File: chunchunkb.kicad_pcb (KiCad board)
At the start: 2 copper layers, 143.7 x 119.1 mm, 124 parts, among them J1 BATT, J2 OLED, SW1 SW_Push, SW10 SW_Push, SW11 SW_Push, SW12 SW_Push, SW13 SW_Push, SW14 SW_Push, SW15 SW_Push, SW16 SW_Push, SW17 SW_Push, SW18 SW_Push, SW19 SW_Push, SW2 SW_Push, SW20 SW_Push, SW21 SW_Push, SW22 SW_Push, SW23 SW_Push, SW24 SW_Push, SW25 SW_Push, SW26 SW_Push, SW27 SW_Push, SW28 SW_Push, SW29 SW_Push, SW3 SW_Push, SW30 SW_Push, SW31 EC11, SW32 SW_Push, SW33 SW_Push, SW34 SW_Push, SW35 SW_Push, SW36 SW_Push, SW4 SW_Push, SW5 SW_Push, SW6 SW_Push, SW7 SW_Push, SW8 SW_Push, SW9 SW_Push

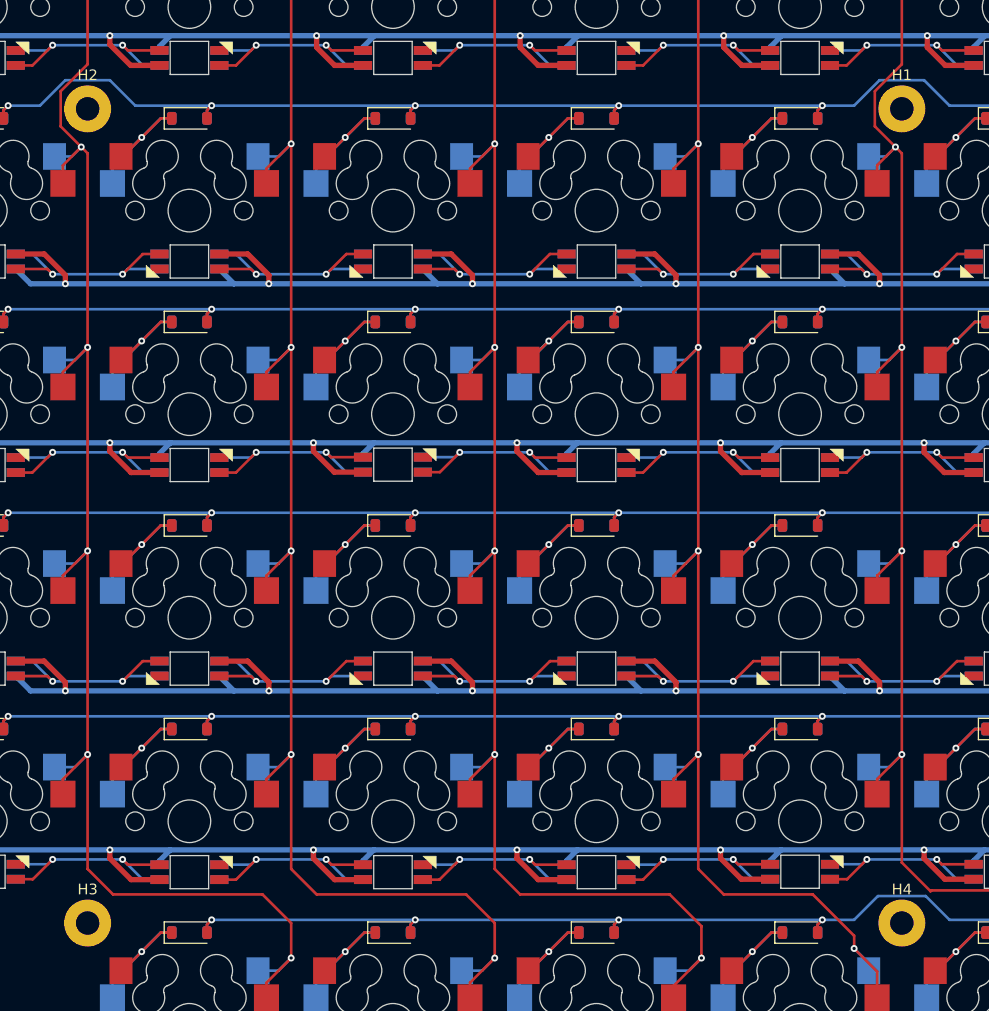
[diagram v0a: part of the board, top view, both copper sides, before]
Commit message: feat: add case
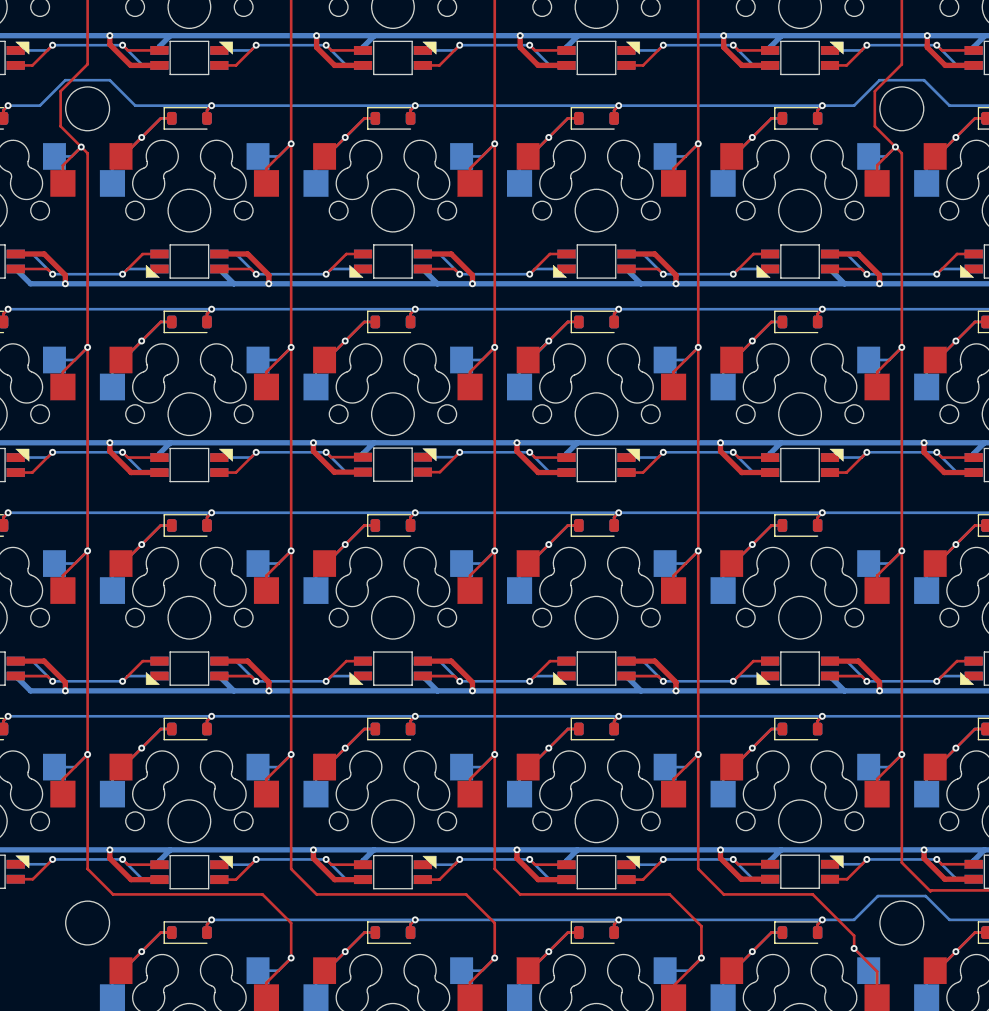
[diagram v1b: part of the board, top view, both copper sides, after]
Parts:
- H1, H2, H3, H4: footprint MountingHole:MountingHole_2.2mm_M2_Pad -> chunchunkb:HOLE_M2_TH

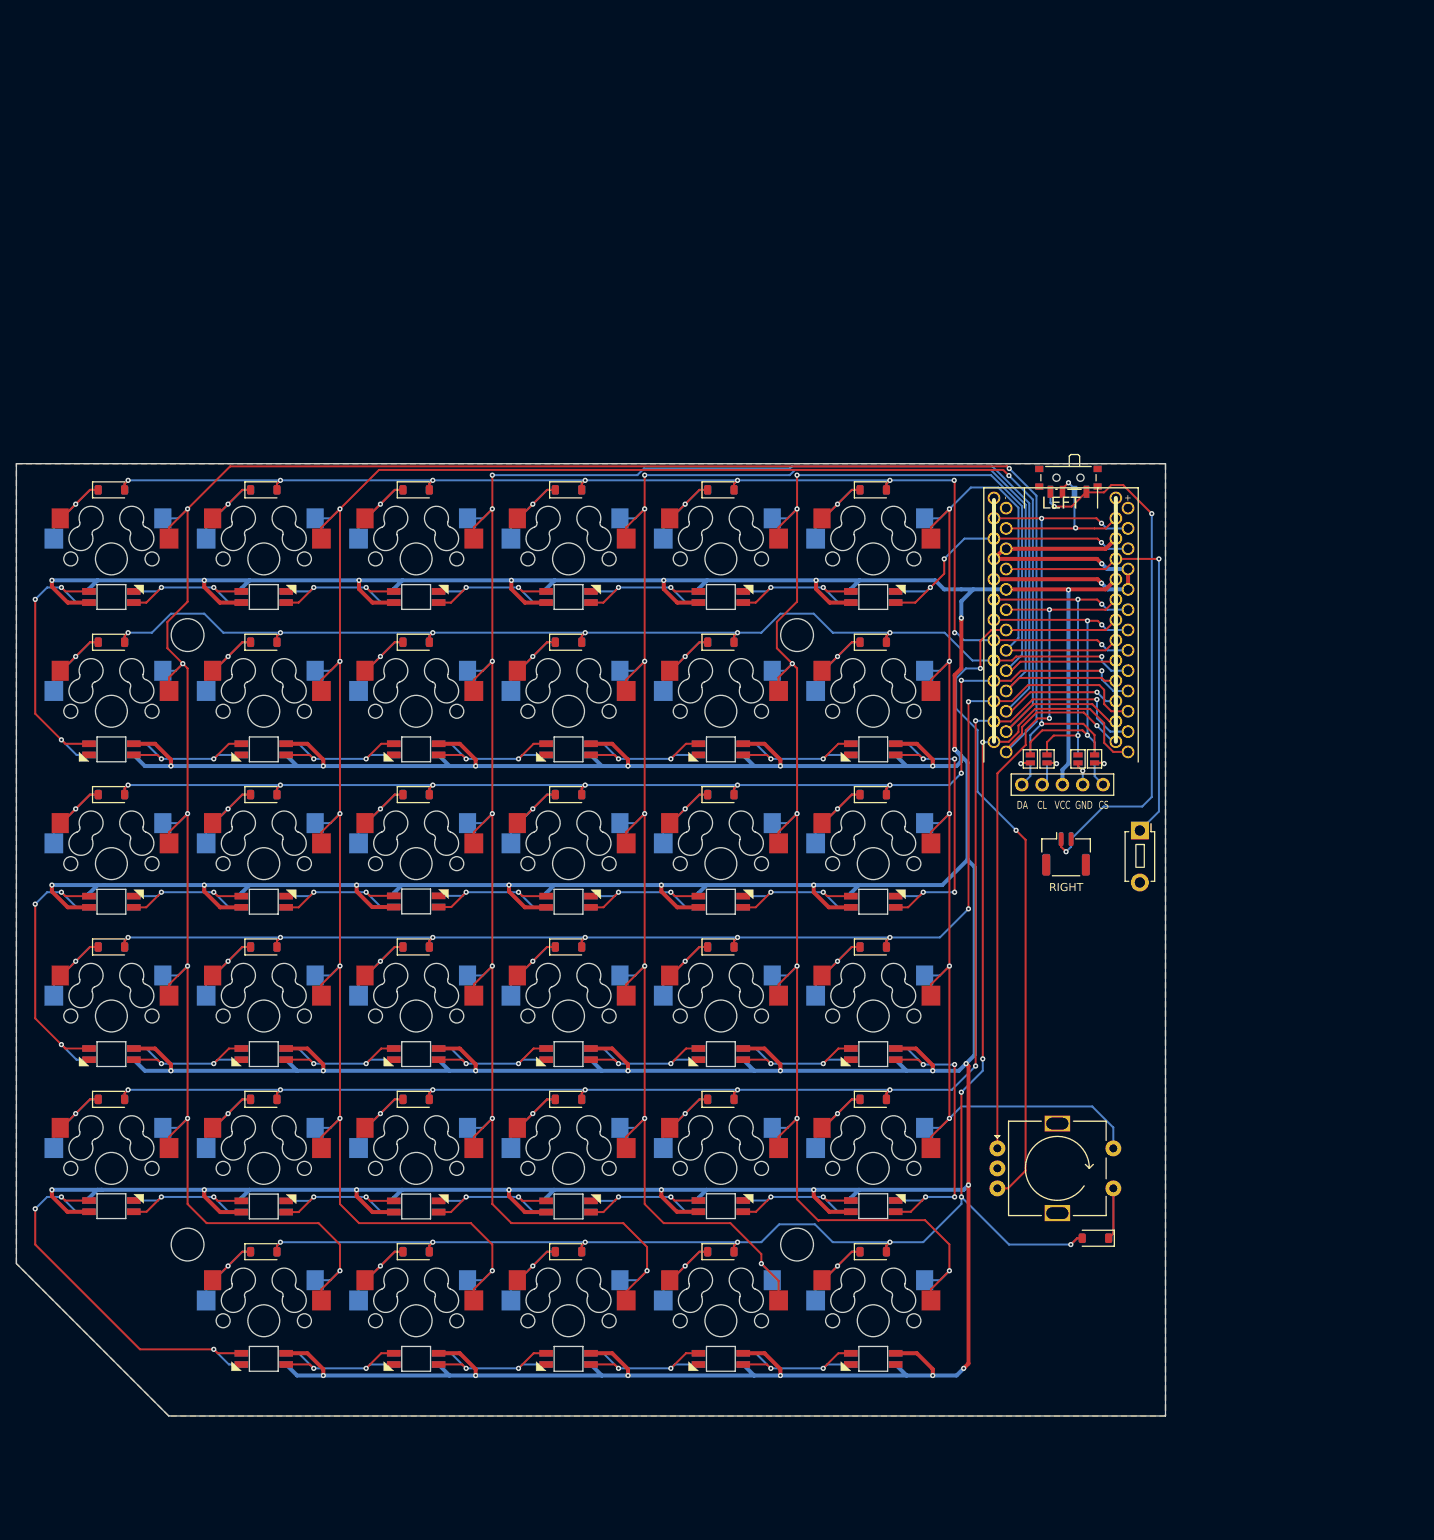
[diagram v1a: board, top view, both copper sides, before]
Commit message: feat: modular layout
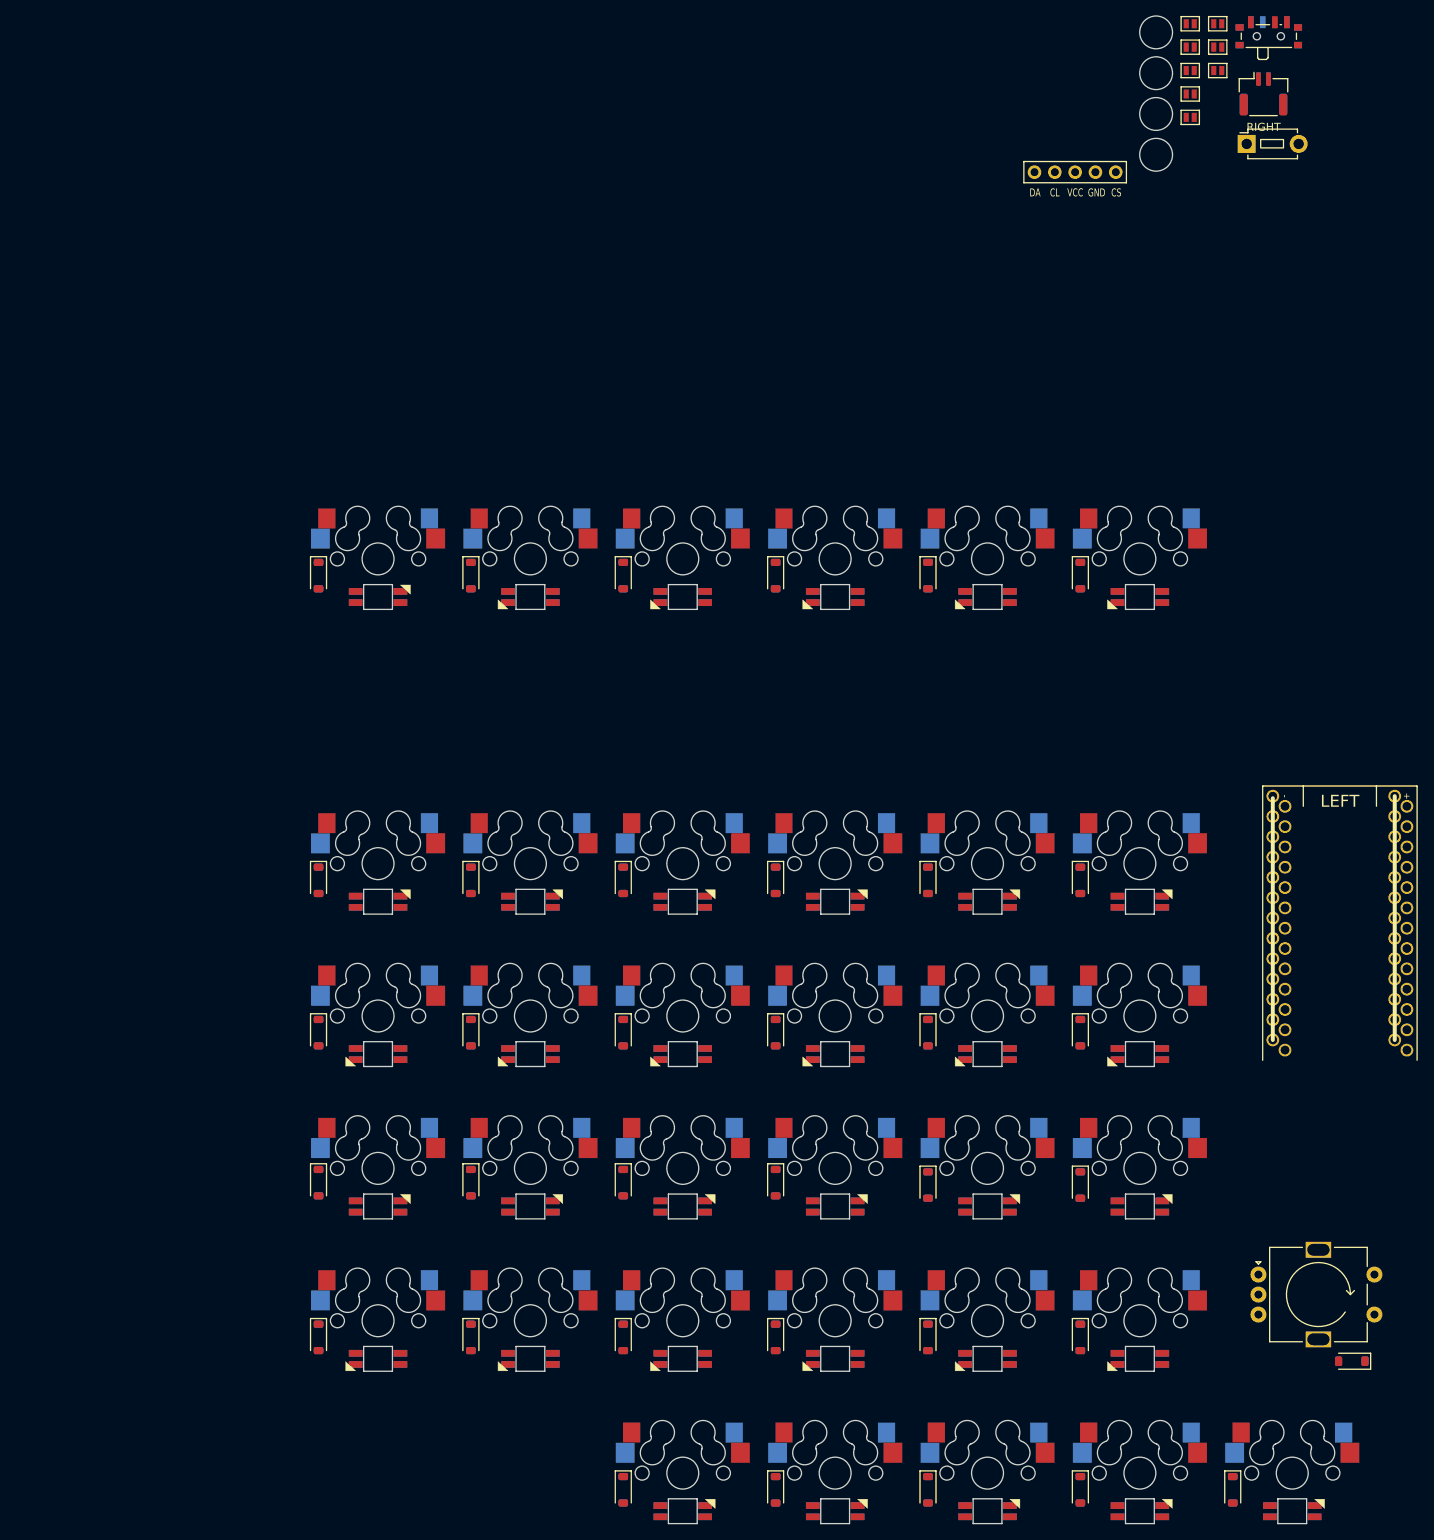
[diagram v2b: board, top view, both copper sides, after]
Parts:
- JP5, JP6, JP7, JP8: moved to F.Cu
- LED10, LED11, LED12, LED19, LED20, LED21, LED22, LED23, LED24, LED31, LED32, LED33, LED34, LED35, LED7, LED8, LED9: moved to B.Cu
- moved H3 186.1 mm to (164.0, -22.3)
- moved H4 143.5 mm to (164.0, -17.2)
- moved H2 140.0 mm to (164.0, -27.4)
- moved LED34 100.9 mm to (142.9, 38.1)
- moved LED31 100.9 mm to (85.7, 38.1)
- moved LED32 100.9 mm to (104.8, 38.1)
- moved LED33 100.9 mm to (123.8, 38.1)
- moved LED35 100.9 mm to (161.9, 38.1)
- moved J1 98.2 mm to (177.4, -24.8)
- moved JP6 94.4 mm to (171.7, -33.6), turned to 0 degrees
- moved JP1 92.7 mm to (168.2, -33.6), turned to 0 degrees
- moved JP7 90.7 mm to (171.7, -30.6), turned to 0 degrees
- moved JP2 90.1 mm to (168.2, -30.6), turned to 0 degrees
- moved JP3 87.9 mm to (168.2, -27.7), turned to 0 degrees
- moved H1 87.7 mm to (164.0, -32.5)
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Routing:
- net VCC: track 1065.2 -> 0.00 mm, vias 41 -> 0
- net COL 5: track 323.1 -> 0.00 mm, vias 8 -> 0
- net COL 4: track 297.5 -> 0.00 mm, vias 7 -> 0
- net COL 3: track 277.5 -> 0.00 mm, vias 8 -> 0
- net COL 2: track 247.5 -> 0.00 mm, vias 7 -> 0
- net COL 1: track 231.0 -> 0.00 mm, vias 7 -> 0
- net ROW 5: track 205.2 -> 0.00 mm, vias 10 -> 0
- net ROW 4: track 190.1 -> 0.00 mm, vias 9 -> 0
- net COL 0: track 185.8 -> 0.00 mm, vias 5 -> 0
- net ROW 3: track 172.1 -> 0.00 mm, vias 8 -> 0
- net ROW 0: track 161.4 -> 0.00 mm, vias 9 -> 0
- net ROW 2: track 155.9 -> 0.00 mm, vias 9 -> 0
- net ROW 1: track 148.1 -> 0.00 mm, vias 7 -> 0
- net ENC B: track 94.6 -> 0.00 mm, vias 2 -> 0
- net ENC A: track 85.2 -> 0.00 mm, vias 2 -> 0
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- removed copper zone on B.Cu, net GND
- removed copper zone on F.Cu, net GND
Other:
- board size 143.7 x 119.1 mm -> 10.6 x 5.5 mm

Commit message: tmp
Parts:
- moved SW_RST1 49.0 mm to (188.8, 28.6)
- moved D10 13.0 mm to (105.1, 63.1), turned to 0 degrees
- moved D7 13.0 mm to (162.2, 63.1), turned to 0 degrees
- moved D8 13.0 mm to (143.2, 63.1), turned to 0 degrees
- moved D9 13.0 mm to (124.1, 63.1), turned to 0 degrees
- moved D12 13.0 mm to (67.0, 63.1), turned to 0 degrees
- moved D11 13.0 mm to (86.0, 63.1), turned to 0 degrees
- moved D13 13.0 mm to (162.2, 82.2), turned to 0 degrees
- moved D1 12.8 mm to (161.9, 25.0), turned to 0 degrees
- moved D3 12.8 mm to (123.8, 25.0), turned to 0 degrees
- moved D4 12.8 mm to (104.8, 25.0), turned to 0 degrees
- moved D5 12.8 mm to (85.7, 25.0), turned to 0 degrees
- moved D6 12.8 mm to (66.7, 25.0), turned to 0 degrees
- moved D15 12.8 mm to (123.8, 82.2), turned to 0 degrees
- moved D16 12.8 mm to (104.8, 82.2), turned to 0 degrees
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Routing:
- net VCC: track 0.00 -> 265.0 mm, vias 0 -> 6
- net ROW 0: track 0.00 -> 133.5 mm, vias 0 -> 6
- net ROW 2: track 0.00 -> 132.6 mm, vias 0 -> 6
- net ROW 1: track 0.00 -> 129.9 mm, vias 0 -> 6
- net Net-(LED34-DOUT): track 0.00 -> 22.9 mm, vias 0 -> 2
- net Net-(LED32-DOUT): track 0.00 -> 22.9 mm, vias 0 -> 2
- net Net-(LED31-DOUT): track 0.00 -> 22.9 mm, vias 0 -> 2
- net Net-(LED33-DOUT): track 0.00 -> 22.9 mm, vias 0 -> 2
- net Net-(LED30-DOUT): track 0.00 -> 22.9 mm, vias 0 -> 2
- net Net-(LED5-DOUT): track 0.00 -> 22.9 mm, vias 0 -> 2
- net Net-(LED3-DOUT): track 0.00 -> 22.9 mm, vias 0 -> 2
- net Net-(LED4-DOUT): track 0.00 -> 22.9 mm, vias 0 -> 2
- net Net-(LED2-DOUT): track 0.00 -> 22.9 mm, vias 0 -> 2
- net Net-(LED7-DOUT): track 0.00 -> 22.9 mm, vias 0 -> 2
- net Net-(LED1-DOUT): track 0.00 -> 22.9 mm, vias 0 -> 2
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- added copper zone on B.Cu, net GND
- added copper zone on F.Cu, net GND
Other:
- board size 10.6 x 5.5 mm -> 152.4 x 142.8 mm
